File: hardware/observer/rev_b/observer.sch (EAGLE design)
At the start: 38 parts, among them J1 CON_HEADER_2X05-SMD+SHROUDED, J2 CON_HEADER_2X05-SMD+SHROUDED, J3 TC2030-CC2538-BL-NL, J4 JUMPER-PTH-2-NO, J5 PINHD-2X8/SMD, J6 CON_HEADER_2X05-PTH+SHROUDED_A, P9/P8 BBB_HEADER, U1 LPS331AP, U2 MPU-9250, U3 SI1147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

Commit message: started routing
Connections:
- new net EEPROM_SCL: P9/P8.I2C2_SCL, U7.SCL
- new net EEPROM_SDA: P9/P8.I2C2_SDA, U7.SDA
- net SCL: no longer P9/P8.I2C2_SCL, U7.SCL
- net SDA: no longer P9/P8.I2C2_SDA, U7.SDA
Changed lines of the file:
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@@
 </segment>
 </net>
-<net name="SDA" class="0">
+<net name="EEPROM_SDA" class="0">
 <segment>
 <pinref part="P9/P8" gate="G$1" pin="I2C2_SDA"/>
@@
 </segment>
 </net>
-<net name="SCL" class="0">
+<net name="EEPROM_SCL" class="0">
 <segment>
 <pinref part="P9/P8" gate="G$1" pin="I2C2_SCL"/>

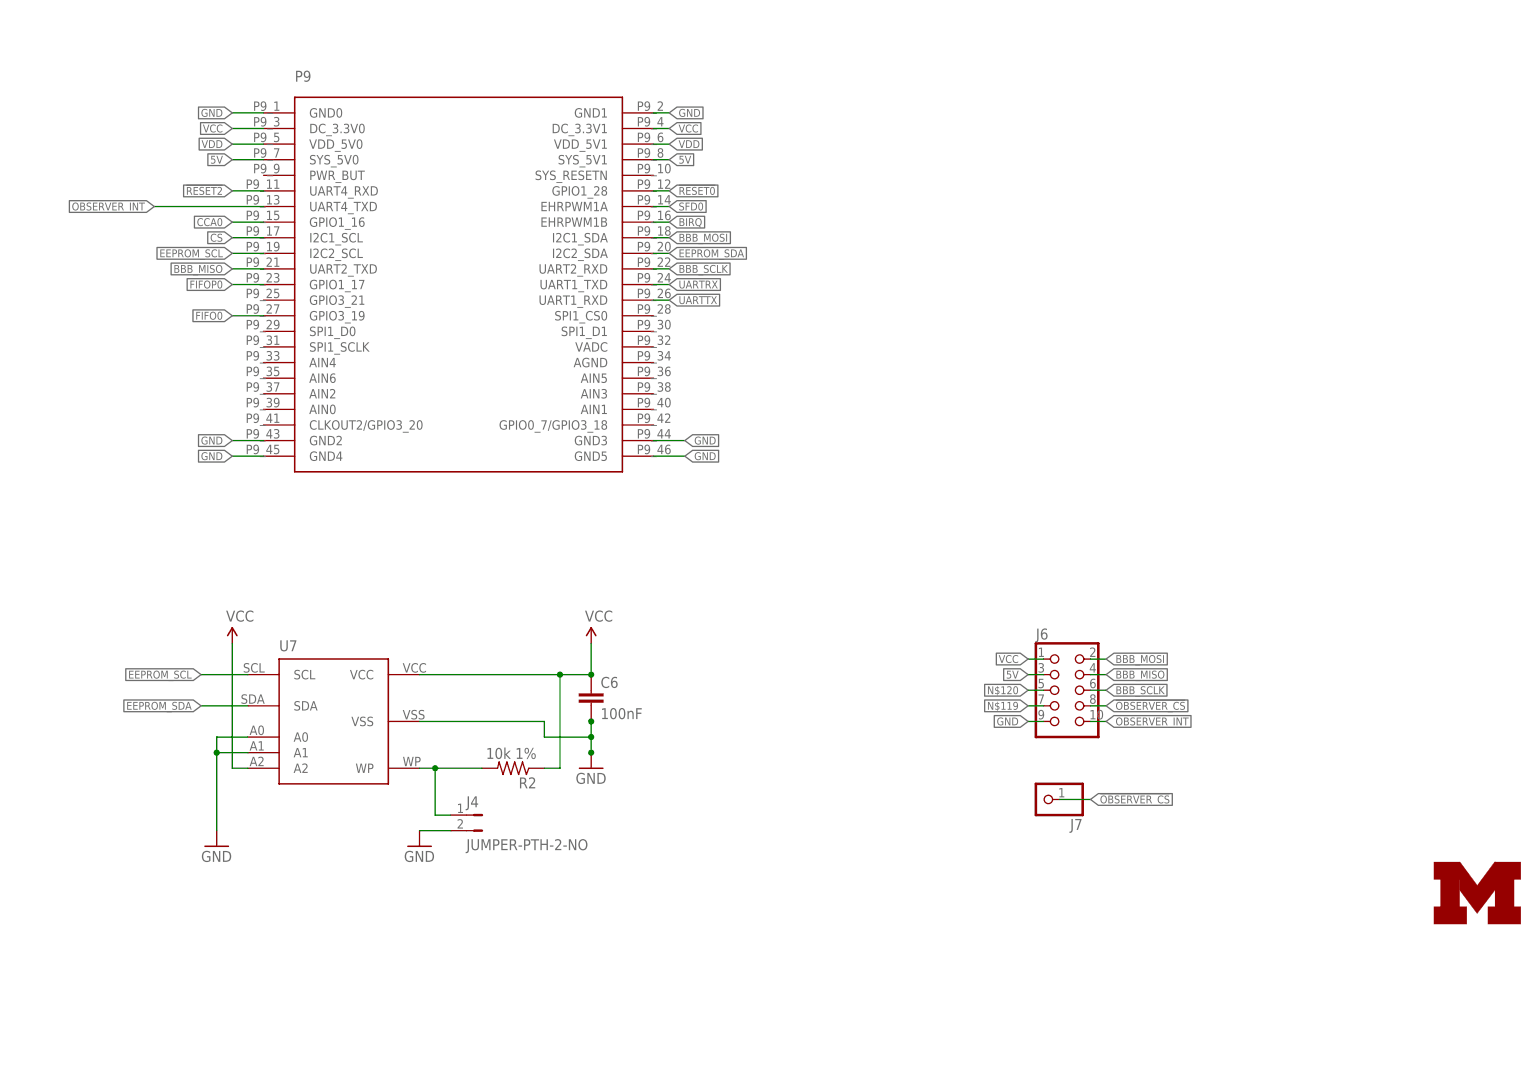
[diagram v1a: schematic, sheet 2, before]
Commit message: added mic and opamp to sch
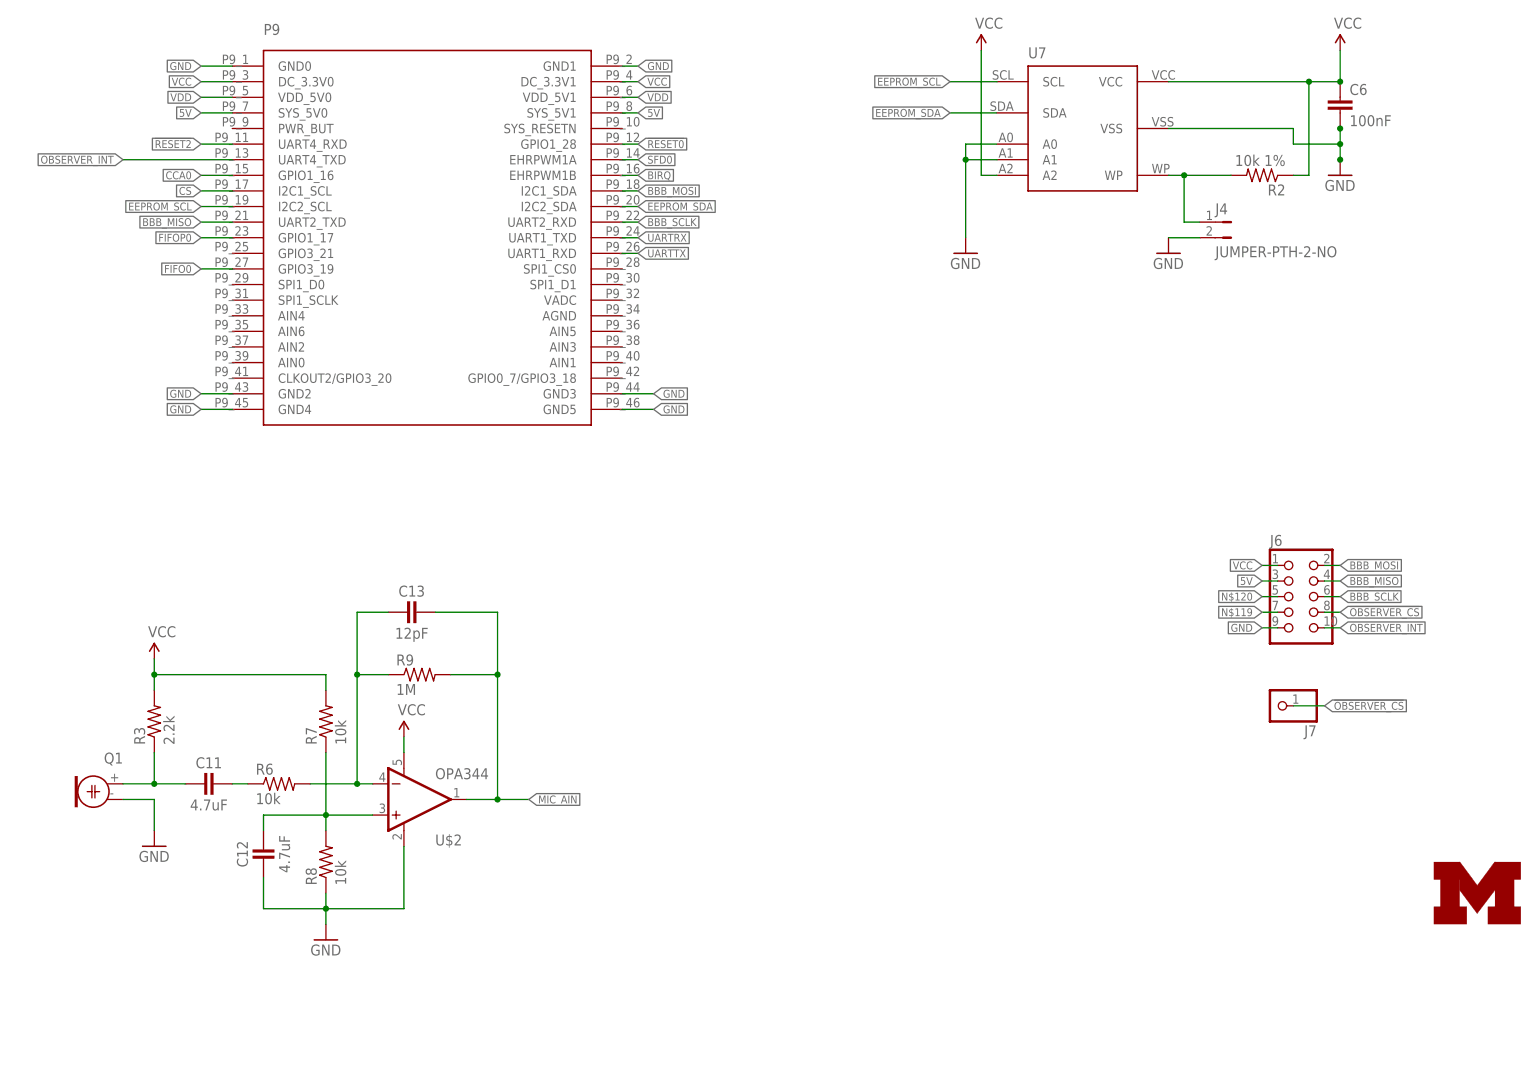
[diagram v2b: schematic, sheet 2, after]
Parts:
- added C11, C12: 4.7uF, passives:CAPACITOR
- added C13: 12pF, passives:CAPACITOR
- added Q1: (no value), observer:ELECTRET
- added R3: 2.2k, passives:RESISTOR0402_RES
- added R6, R7, R8: 10k, passives:RESISTOR0402_RES
- added R9: 1M, passives:RESISTOR0402_RES
- added U$2: OPA344, SparkFun-AnalogIC:OPA344
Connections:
- net UN renamed MIC_INT
- new net MIC_AIN: C13.1, R9.2, U$2.OUT
- new net N$1: C11.2, Q1.2, R3.1
- new net N$10: C12.1, R7.1, R8.2, U$2.+IN
- new net N$5: C11.1, R6.1
- new net N$9: R6.2, R9.1, U$2.-IN
- net GND: now also C12.2, Q1.1, R8.1, U$2.V-
- net VCC: now also R3.2, R7.2, U$2.V+
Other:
- moved on the sheet: C6, J4, J6, J7, R2, U7

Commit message: Finished routing, needs to be looked over for correctness
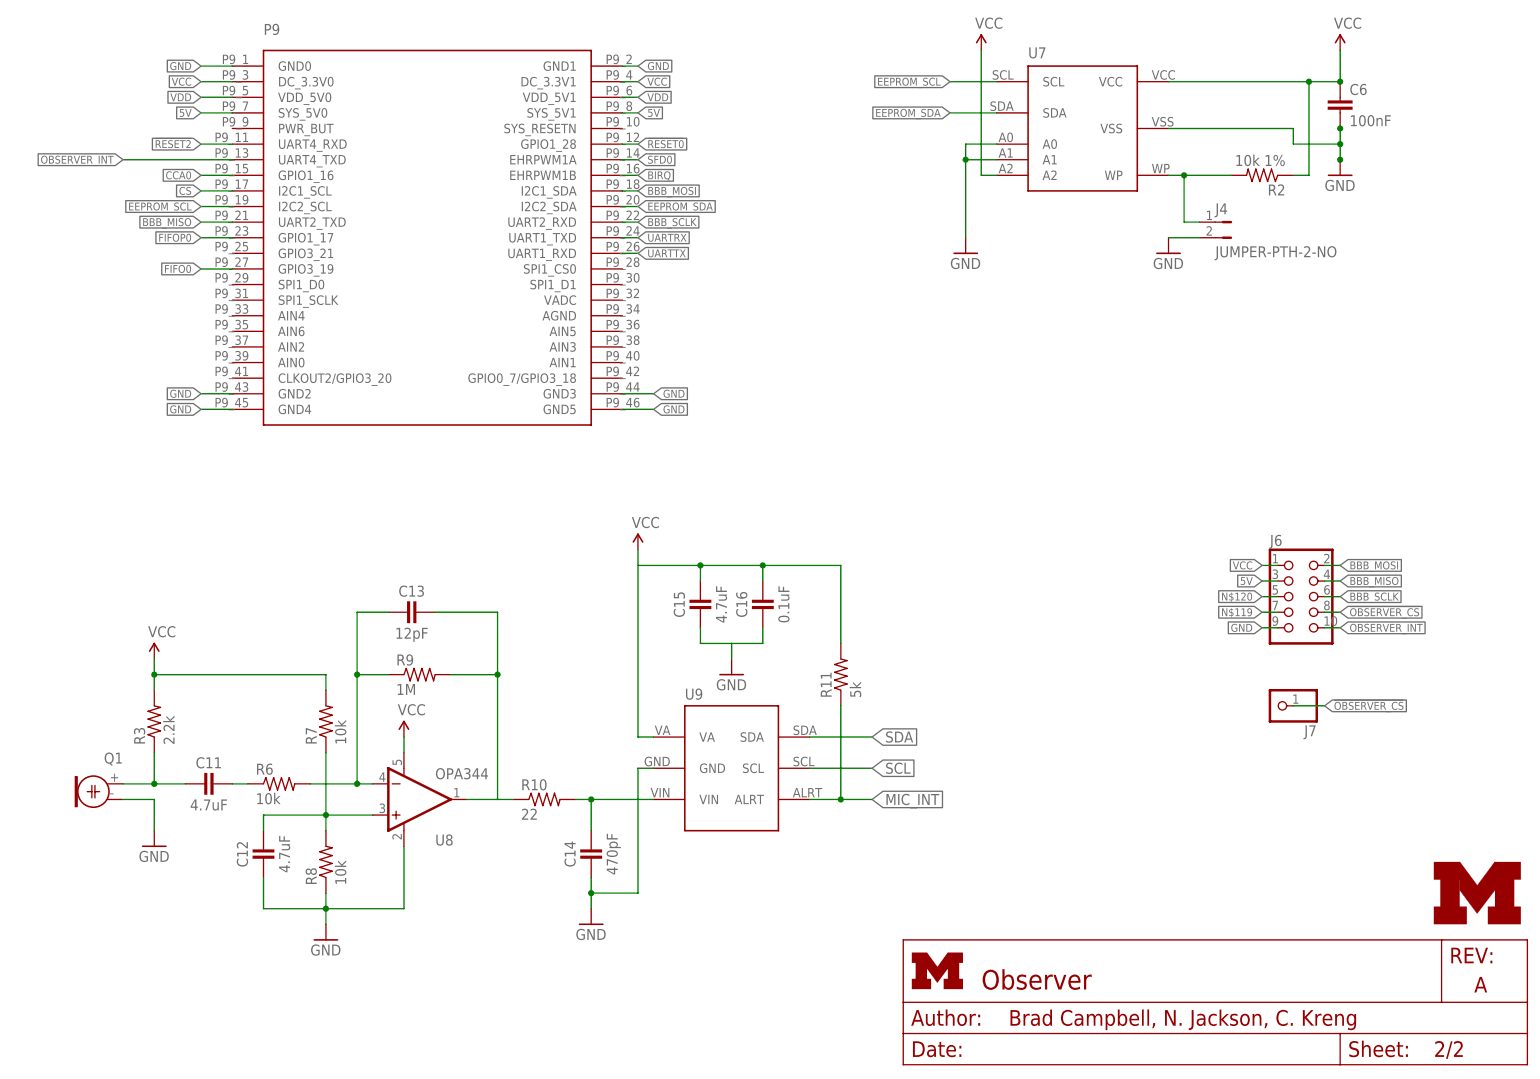
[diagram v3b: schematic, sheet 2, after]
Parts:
- added C14: 470pF, passives:CAPACITOR
- added C15: 4.7uF, passives:CAPACITOR
- added C16: 0.1uF, passives:CAPACITOR
- added R10: 22, passives:RESISTOR0402_RES
- added R11: 5k, passives:RESISTOR0402_RES
- added U9: ADC121C021, observer:ADC121C021
- renumbered U$2 to U8
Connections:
- new net N$11: C14.1, R10.2, U9.VIN
- net GND: now also C14.2, C15.2, C16.2, U9.GND
- net MIC_AIN: now also R10.1
- net MIC_INT: now also R11.1, U9.ALRT
- net SCL: now also U9.SCL
- net SDA: now also U9.SDA
- net VCC: now also C15.1, C16.1, R11.2, U9.VA
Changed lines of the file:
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@@
 <part name="J7" library="pinhead" deviceset="PINHD-1X1" device=""/>
 <part name="Q1" library="observer" deviceset="ELECTRET" device=""/>
-<part name="U$2" library="SparkFun-AnalogIC" deviceset="OPA344" device=""/>
+<part name="U8" library="SparkFun-AnalogIC" deviceset="OPA344" device=""/>
 <part name="R3" library="passives" deviceset="RESISTOR" device="0402_RES" value="2.2k"/>
 <part name="SUPPLY3" library="SparkFun-Aesthetics" deviceset="VCC" device=""/>
@@
 <part name="R9" library="passives" deviceset="RESISTOR" device="0402_RES" value="1M"/>
 <part name="C13" library="passives" deviceset="CAPACITOR" device="" value="12pF"/>
+<part name="U9" library="observer" deviceset="ADC121C021" device=""/>
+<part name="R10" library="passives" deviceset="RESISTOR" device="0402_RES" value="22"/>
+<part name="C14" library="passives" deviceset="CAPACITOR" device="" value="470pF"/>
+<part name="GND25" library="SparkFun-Aesthetics" deviceset="GND" device=""/>
+<part name="SUPPLY5" library="SparkFun-Aesthetics" deviceset="VCC" device=""/>
+<part name="C15" library="passives" deviceset="CAPACITOR" device="" value="4.7uF"/>
+<part name="C16" library="passives" deviceset="CAPACITOR" device="" value="0.1uF"/>
+<part name="R11" library="passives" deviceset="RESISTOR" device="0402_RES" value="5k"/>
+<part name="GND26" library="SparkFun-Aesthetics" deviceset="GND" device=""/>
 </parts>
 <sheets>
@@
 <instance part="J7" gate="G$1" x="208.28" y="58.42" rot="R180"/>
 <instance part="Q1" gate="G$1" x="17.78" y="43.18" rot="R180"/>
-<instance part="U$2" gate="G$1" x="66.04" y="43.18"/>
+<instance part="U8" gate="G$1" x="66.04" y="43.18"/>
 <instance part="R3" gate="G$1" x="25.4" y="55.88" rot="R90"/>
 <instance part="SUPPLY3" gate="G$1" x="25.4" y="66.04"/>
@@
 <instance part="R9" gate="G$1" x="68.58" y="63.5"/>
 <instance part="C13" gate="G$1" x="68.58" y="73.66" rot="R270"/>
+<instance part="U9" gate="G$1" x="111.76" y="38.1"/>
+<instance part="R10" gate="G$1" x="88.9" y="43.18"/>
+<instance part="C14" gate="G$1" x="96.52" y="35.56"/>
+<instance part="GND25" gate="1" x="96.52" y="22.86"/>
+<instance part="SUPPLY5" gate="G$1" x="104.14" y="83.82"/>
+<instance part="C15" gate="G$1" x="114.3" y="76.2"/>
+<instance part="C16" gate="G$1" x="124.46" y="76.2"/>
+<instance part="R11" gate="G$1" x="137.16" y="63.5" rot="R90"/>
+<instance part="GND26" gate="1" x="119.38" y="63.5"/>
 </instances>
 <busses>
@@
 <wire x1="53.34" y1="27.94" x2="53.34" y2="25.4" width="0.1524" layer="91"/>
 <pinref part="GND24" gate="1" pin="GND"/>
-<pinref part="U$2" gate="G$1" pin="V-"/>
+<pinref part="U8" gate="G$1" pin="V-"/>
 <wire x1="53.34" y1="25.4" x2="53.34" y2="22.86" width="0.1524" layer="91"/>
 <wire x1="66.04" y1="35.56" x2="66.04" y2="25.4" width="0.1524" layer="91"/>
 <wire x1="66.04" y1="25.4" x2="53.34" y2="25.4" width="0.1524" layer="91"/>
 <junction x="53.34" y="25.4"/>
+</segment>
+<segment>
+<pinref part="GND25" gate="1" pin="GND"/>
+<pinref part="C14" gate="G$1" pin="2"/>
+<wire x1="96.52" y1="25.4" x2="96.52" y2="27.94" width="0.1524" layer="91"/>
+<pinref part="U9" gate="G$1" pin="GND"/>
+<wire x1="96.52" y1="27.94" x2="96.52" y2="30.48" width="0.1524" layer="91"/>
+<wire x1="106.68" y1="48.26" x2="104.14" y2="48.26" width="0.1524" layer="91"/>
+<wire x1="104.14" y1="48.26" x2="104.14" y2="27.94" width="0.1524" layer="91"/>
+<wire x1="104.14" y1="27.94" x2="96.52" y2="27.94" width="0.1524" layer="91"/>
+<junction x="96.52" y="27.94"/>
+</segment>
+<segment>
+<pinref part="C15" gate="G$1" pin="2"/>
+<wire x1="114.3" y1="71.12" x2="114.3" y2="68.58" width="0.1524" layer="91"/>
+<pinref part="C16" gate="G$1" pin="2"/>
+<wire x1="124.46" y1="68.58" x2="124.46" y2="71.12" width="0.1524" layer="91"/>
+<wire x1="114.3" y1="68.58" x2="119.38" y2="68.58" width="0.1524" layer="91"/>
+<pinref part="GND26" gate="1" pin="GND"/>
+<wire x1="124.46" y1="68.58" x2="119.38" y2="68.58" width="0.1524" layer="91"/>
+<wire x1="119.38" y1="68.58" x2="119.38" y2="66.04" width="0.1524" layer="91"/>
 </segment>
 </net>
@@
 </segment>
 <segment>
-<pinref part="U$2" gate="G$1" pin="V+"/>
+<pinref part="U8" gate="G$1" pin="V+"/>
 <pinref part="SUPPLY4" gate="G$1" pin="VCC"/>
 <wire x1="66.04" y1="50.8" x2="66.04" y2="53.34" width="0.1524" layer="91"/>
+</segment>
+<segment>
+<pinref part="U9" gate="G$1" pin="VA"/>
+<wire x1="106.68" y1="53.34" x2="104.14" y2="53.34" width="0.1524" layer="91"/>
+<wire x1="104.14" y1="53.34" x2="104.14" y2="81.28" width="0.1524" layer="91"/>
+<pinref part="SUPPLY5" gate="G$1" pin="VCC"/>
+<wire x1="104.14" y1="83.82" x2="104.14" y2="81.28" width="0.1524" layer="91"/>
+<wire x1="104.14" y1="81.28" x2="114.3" y2="81.28" width="0.1524" layer="91"/>
+<wire x1="114.3" y1="78.74" x2="114.3" y2="81.28" width="0.1524" layer="91"/>
+<wire x1="114.3" y1="81.28" x2="124.46" y2="81.28" width="0.1524" layer="91"/>
+<wire x1="124.46" y1="81.28" x2="124.46" y2="78.74" width="0.1524" layer="91"/>
+<pinref part="C15" gate="G$1" pin="1"/>
+<pinref part="C16" gate="G$1" pin="1"/>
+<junction x="114.3" y="81.28"/>
+<pinref part="R11" gate="G$1" pin="2"/>
+<wire x1="137.16" y1="68.58" x2="137.16" y2="81.28" width="0.1524" layer="91"/>
+<wire x1="137.16" y1="81.28" x2="124.46" y2="81.28" width="0.1524" layer="91"/>
+<junction x="124.46" y="81.28"/>
 </segment>
 </net>
@@
 <segment>
 <pinref part="R6" gate="G$1" pin="2"/>
-<pinref part="U$2" gate="G$1" pin="-IN"/>
+<pinref part="U8" gate="G$1" pin="-IN"/>
 <wire x1="50.8" y1="45.72" x2="58.42" y2="45.72" width="0.1524" layer="91"/>
 <wire x1="58.42" y1="45.72" x2="60.96" y2="45.72" width="0.1524" layer="91"/>
@@
 <pinref part="C12" gate="G$1" pin="1"/>
 <junction x="53.34" y="40.64"/>
-<pinref part="U$2" gate="G$1" pin="+IN"/>
+<pinref part="U8" gate="G$1" pin="+IN"/>
 <wire x1="60.96" y1="40.64" x2="53.34" y2="40.64" width="0.1524" layer="91"/>
 </segment>
@@
 <wire x1="71.12" y1="73.66" x2="81.28" y2="73.66" width="0.1524" layer="91"/>
 <wire x1="81.28" y1="73.66" x2="81.28" y2="63.5" width="0.1524" layer="91"/>
-<pinref part="U$2" gate="G$1" pin="OUT"/>
+<pinref part="U8" gate="G$1" pin="OUT"/>
 <wire x1="81.28" y1="63.5" x2="81.28" y2="43.18" width="0.1524" layer="91"/>
 <wire x1="81.28" y1="43.18" x2="76.2" y2="43.18" width="0.1524" layer="91"/>
@@
 <wire x1="73.66" y1="63.5" x2="81.28" y2="63.5" width="0.1524" layer="91"/>
 <junction x="81.28" y="63.5"/>
-<junction x="81.28" y="43.18"/>
-<wire x1="81.28" y1="43.18" x2="86.36" y2="43.18" width="0.1524" layer="91"/>
-<label x="86.36" y="43.18" size="1.27" layer="95" xref="yes"/>
-</segment>
-</net>
+<pinref part="R10" gate="G$1" pin="1"/>
+<wire x1="81.28" y1="43.18" x2="83.82" y2="43.18" width="0.1524" layer="91"/>
+</segment>
+</net>
+<net name="N$11" class="0">
+<segment>
+<pinref part="R10" gate="G$1" pin="2"/>
+<pinref part="U9" gate="G$1" pin="VIN"/>
+<wire x1="93.98" y1="43.18" x2="96.52" y2="43.18" width="0.1524" layer="91"/>
+<pinref part="C14" gate="G$1" pin="1"/>
+<wire x1="96.52" y1="43.18" x2="106.68" y2="43.18" width="0.1524" layer="91"/>
+<wire x1="96.52" y1="38.1" x2="96.52" y2="43.18" width="0.1524" layer="91"/>
+<junction x="96.52" y="43.18"/>
+</segment>
+</net>
+<net name="SDA" class="0">
+<segment>
+<pinref part="U9" gate="G$1" pin="SDA"/>
+<wire x1="132.08" y1="53.34" x2="142.24" y2="53.34" width="0.1524" layer="91"/>
+<label x="142.24" y="53.34" size="1.778" layer="95" xref="yes"/>
+</segment>
+</net>
+<net name="SCL" class="0">
+<segment>
+<pinref part="U9" gate="G$1" pin="SCL"/>
+<wire x1="132.08" y1="48.26" x2="142.24" y2="48.26" width="0.1524" layer="91"/>
+<label x="142.24" y="48.26" size="1.778" layer="95" xref="yes"/>
+</segment>
+</net>
+<net name="MIC_INT" class="0">
+<segment>
+<pinref part="U9" gate="G$1" pin="ALRT"/>
+<wire x1="132.08" y1="43.18" x2="137.16" y2="43.18" width="0.1524" layer="91"/>
+<wire x1="137.16" y1="43.18" x2="137.16" y2="58.42" width="0.1524" layer="91"/>
+<wire x1="137.16" y1="43.18" x2="142.24" y2="43.18" width="0.1524" layer="91"/>
+<pinref part="R11" gate="G$1" pin="1"/>
+<junction x="137.16" y="43.18"/>
+<label x="142.24" y="43.18" size="1.778" layer="95" xref="yes"/>
+</segment>
+</net>
